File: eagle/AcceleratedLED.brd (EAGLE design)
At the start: 19 parts, among them Q1 16MHZ, U1 ATMEGA328, U8 TXB0108PWR

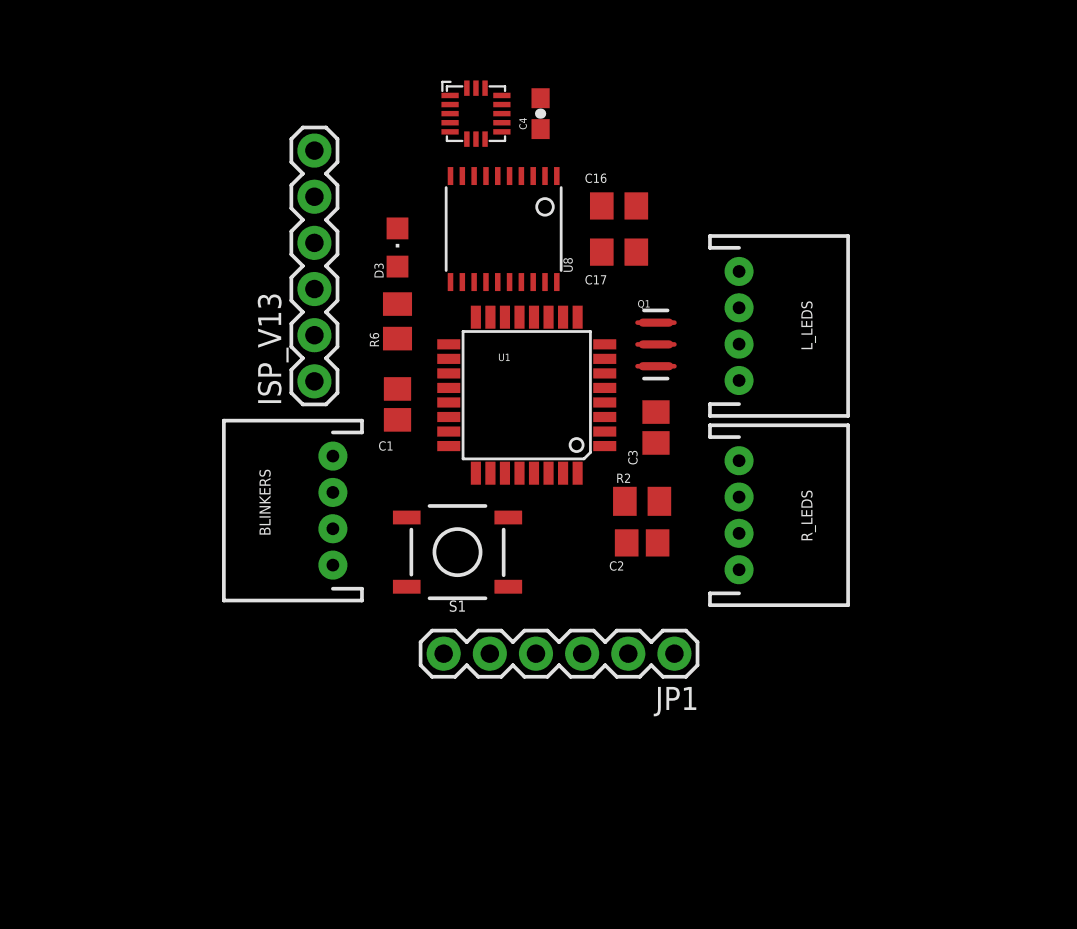
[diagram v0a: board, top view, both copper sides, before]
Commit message: Add switching power
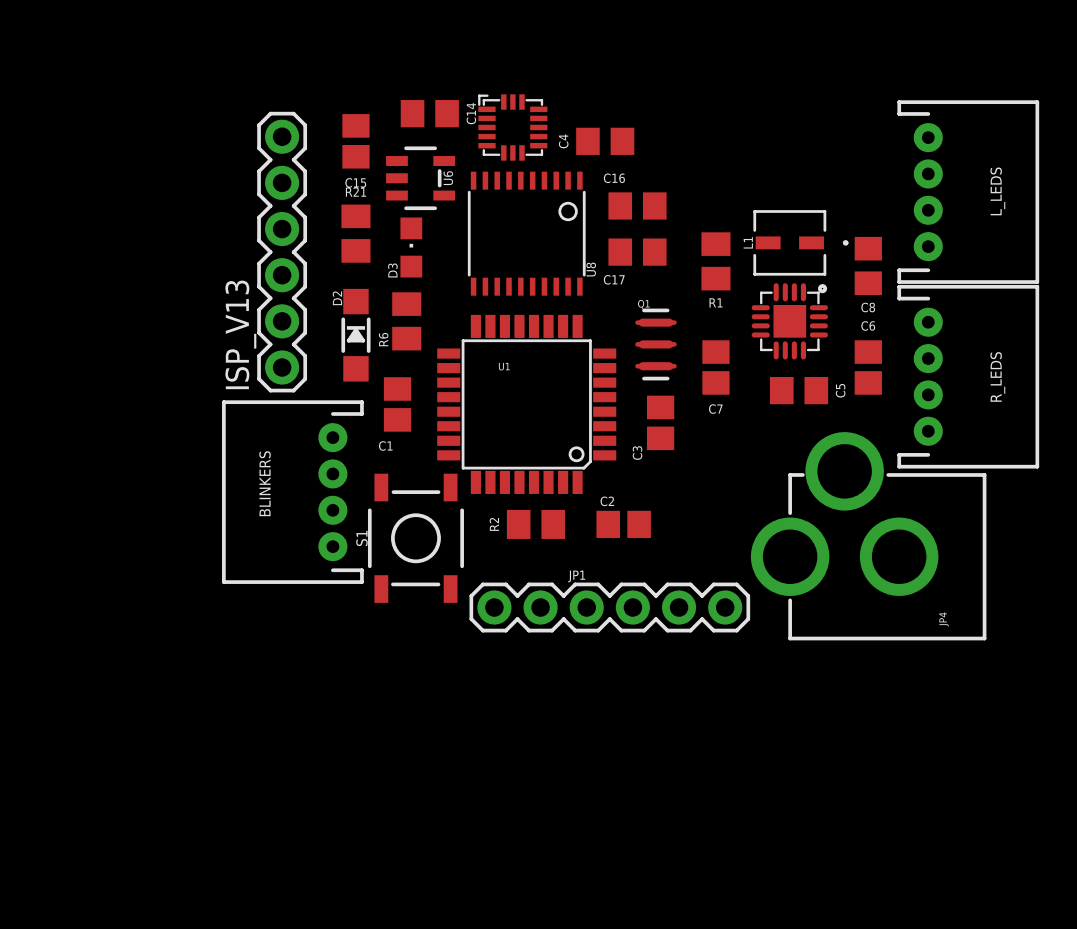
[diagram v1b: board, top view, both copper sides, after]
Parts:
- added C14, C5: 10uF, RemoteMotion:C0805
- added C15: 10uF, MotionSign:C0805
- added C6: 0.1uF, MotionSign:C0805
- added C7: 3.3nF, MotionSign:C0805
- added C8: 22uF, RemoteMotion:C0805
- added D2: MBR120, MotionSign:SOD-123
- added IC1: TPS62133, robopoly:QFN16
- added JP4: POWER_JACKPTH, MotionSign:POWER_JACK_PTH
- added L1: 2.2μH, bg_eagle_lib:IND_IHLP-1212BZ-L
- added R1: 100K, MotionSign:M0805
- added R21: 10K, MotionSign:M0805
- added U6: SPX3819, MotionSign:SOT23-5
- C4: device SparkFun-Capacitors:0603-CAP -> RemoteMotion:C0805
- moved R_LEDS 12.9 mm to (50.0, 27.7)
- moved L_LEDS 12.8 mm to (50.0, 37.8)
- moved R2 5.98 mm to (28.4, 19.6)
- moved C4 3.87 mm to (32.3, 40.6), turned to 0 degrees
- moved JP1 3.78 mm to (38.9, 15.0)
- moved S1 2.41 mm to (21.8, 18.8), turned to 90 degrees
- moved U2 2.17 mm to (27.2, 41.4)
- moved ISP_V13 1.93 mm to (14.5, 28.2)
- moved C2 1.44 mm to (33.3, 19.6)
- moved U8 1.30 mm to (27.9, 35.6)
- moved BLINKERS 1.02 mm to (17.3, 21.3)
- moved C16 1.02 mm to (34.0, 37.1)
- moved C17 1.02 mm to (34.0, 34.5)
- moved D3 0.76 mm to (21.6, 34.8)
- moved U1 0.51 mm to (27.9, 26.2)
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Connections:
- new net LDO_EN: R21.2, U6.3
- new net N$23: C15.1, D2.C, R21.1, U6.1
- new net PG: IC1.4, R1.2
- new net RAW: C5.1, C6.1, IC1.10, IC1.11, IC1.12, IC1.13, JP4.PWR
- new net SS/TR: C7.1, IC1.9
- new net SW: IC1.1, IC1.2, IC1.3, L1.2
- net 3.3V: now also C14.1, C4.1, U6.5; no longer C4.2
- net AREF: now also C1.1; no longer C1.2
- net GND: now also C1.2, C14.2, C15.2, C3.2, C4.2, C5.2, C6.2, C7.2, C8.2, IC1.15, IC1.16, IC1.5, IC1.6, IC1.7, IC1.8, IC1.PAD, JP4.GND, U6.2; no longer C1.1, C3.1, C4.1
- net VCC: now also C3.1, C8.1, D2.A, IC1.14, L1.1, R1.1; no longer C3.2

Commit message: changes
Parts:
- BLINKERS: device MotionSign:JST-4-PTH -> SparkFun-Connectors:JST-3-PTH
- moved JP1 5.71 mm to (33.5, 13.0)
- moved L_LEDS 2.09 mm to (48.0, 38.4)
- moved JP4 2.03 mm to (54.1, 17.8)
- moved R_LEDS 2.03 mm to (48.0, 27.7)
- moved C6 1.78 mm to (45.0, 28.2)
- moved C8 1.78 mm to (45.0, 33.8)
- moved C5 1.30 mm to (41.7, 27.2)
- moved BLINKERS 1.27 mm to (16.3, 22.1)
- moved IC1 1.02 mm to (41.4, 30.7)
- moved R1 0.92 mm to (37.8, 33.3)
- moved L1 0.76 mm to (41.7, 35.1)
- moved C7 0.57 mm to (37.8, 27.9)
- moved Q1 0.51 mm to (34.5, 29.5)
- moved C17 0.51 mm to (34.0, 34.0)
- moved C3 0.51 mm to (34.8, 25.1)
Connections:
- net L_BO renamed L_SCK
- net L_DO renamed L_DATA
- net R_BO renamed R_SCK
- net R_DO renamed R_DATA
- net VCC: no longer BLINKERS.4

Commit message: small board changes
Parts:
- added EFFECT_LEDS: (no value), MotionSign:JST-4-PTH
- moved L_LEDS 1.85 mm to (49.8, 37.8)
- moved JP4 1.78 mm to (55.9, 17.8)
- moved R_LEDS 1.78 mm to (49.8, 27.7)
- moved ISP_V13 1.52 mm to (13.0, 28.2)
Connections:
- removed net D8: U1.12
- removed net D9: U1.13
- new net E_DATA: EFFECT_LEDS.3, U1.12
- new net E_SCK: EFFECT_LEDS.2, U1.13
- net GND: now also EFFECT_LEDS.1
- net VCC: now also EFFECT_LEDS.4

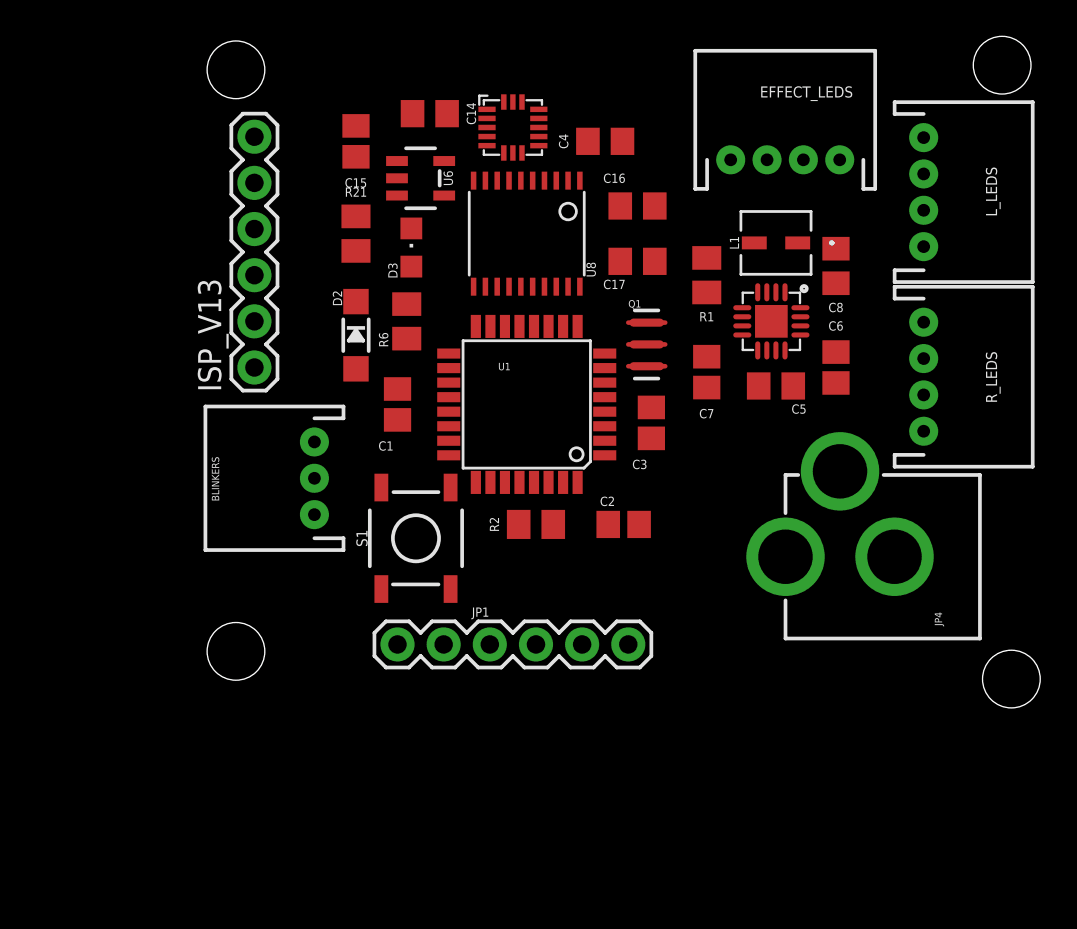
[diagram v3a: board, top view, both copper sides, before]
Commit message: Move to support R1,L1,R2,L2 strands
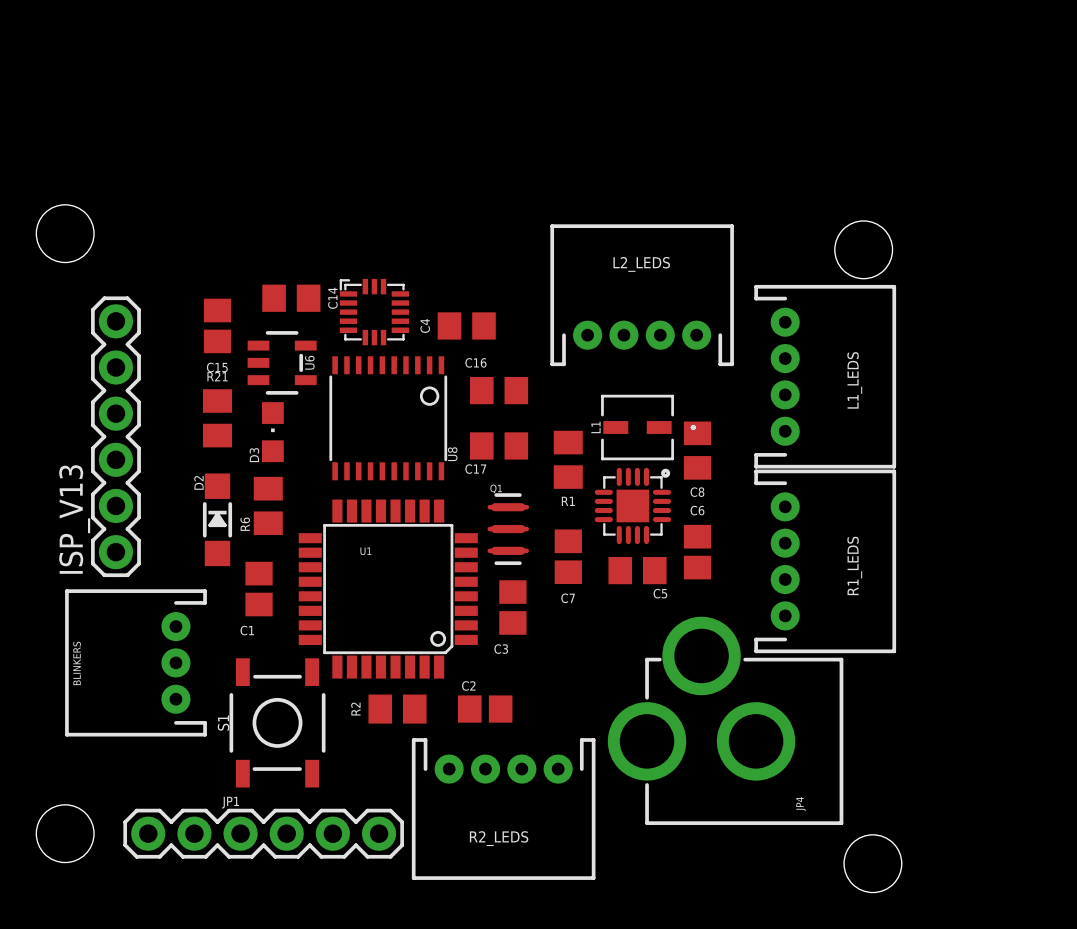
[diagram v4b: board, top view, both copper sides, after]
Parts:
- removed EFFECT_LEDS, L_LEDS, R_LEDS: (no value), MotionSign:JST-4-PTH
- added L1_LEDS, L2_LEDS, R1_LEDS, R2_LEDS: (no value), MotionSign:JST-4-PTH
- moved JP1 17.2 mm to (19.8, 2.54)
- moved C14 12.7 mm to (15.0, 32.0)
- moved C16 12.7 mm to (26.4, 26.9)
- moved IC1 12.7 mm to (33.8, 20.6)
- moved JP4 12.7 mm to (48.3, 7.62)
- moved R21 12.7 mm to (10.9, 25.4)
- moved U8 12.7 mm to (20.3, 25.4)
- moved BLINKERS 12.7 mm to (8.64, 11.9)
- moved C1 12.7 mm to (13.2, 16.0)
- moved C15 12.7 mm to (10.9, 30.5)
- moved C17 12.7 mm to (26.4, 23.9)
- moved C2 12.7 mm to (25.7, 9.40)
- moved C3 12.7 mm to (27.2, 15.0)
- moved C4 12.7 mm to (24.6, 30.5)
- moved D2 12.7 mm to (10.9, 19.8)
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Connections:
- removed net A2: U1.25
- removed net A3: U1.26
- removed net E_DATA: EFFECT_LEDS.3, U1.12
- removed net E_SCK: EFFECT_LEDS.2, U1.13
- removed net L_DATA: L_LEDS.3, U1.10
- removed net L_SCK: L_LEDS.2, U1.11
- removed net R_DATA: R_LEDS.3, U1.2
- removed net R_SCK: R_LEDS.2, U1.9
- new net L1_DATA: L1_LEDS.3, U1.10
- new net L1_SCK: L1_LEDS.2, U1.11
- new net L2_DATA: L2_LEDS.3, U1.12
- new net L2_SCK: L2_LEDS.2, U1.13
- new net R1_DATA: R1_LEDS.3, U1.2
- new net R1_SCK: R1_LEDS.2, U1.9
- new net R2_DATA: R2_LEDS.3, U1.25
- new net R2_SCK: R2_LEDS.2, U1.26
- net GND: now also L1_LEDS.1, L2_LEDS.1, R1_LEDS.1, R2_LEDS.1; no longer EFFECT_LEDS.1, L_LEDS.1, R_LEDS.1
- net VCC: now also L1_LEDS.4, L2_LEDS.4, R1_LEDS.4, R2_LEDS.4; no longer EFFECT_LEDS.4, L_LEDS.4, R_LEDS.4
